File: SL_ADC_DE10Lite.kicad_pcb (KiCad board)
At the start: 4 copper layers, 25 parts, among them J1 DE10Lite header, J2 Conn_02x08_Odd_Even, J3 Digital ground header, J4 Analog header, J5 Power header

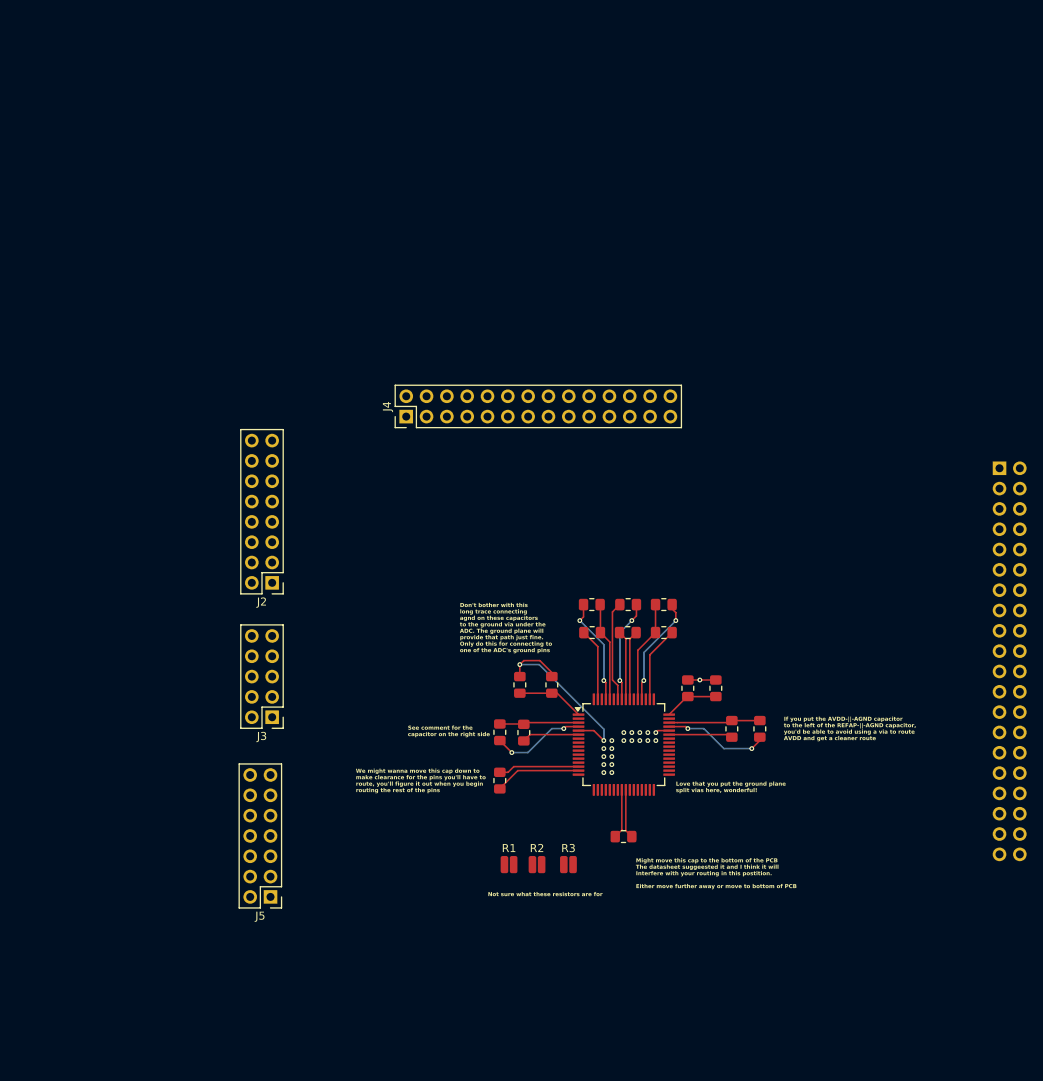
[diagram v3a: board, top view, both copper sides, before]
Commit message: Add De10lite dimensions and routes
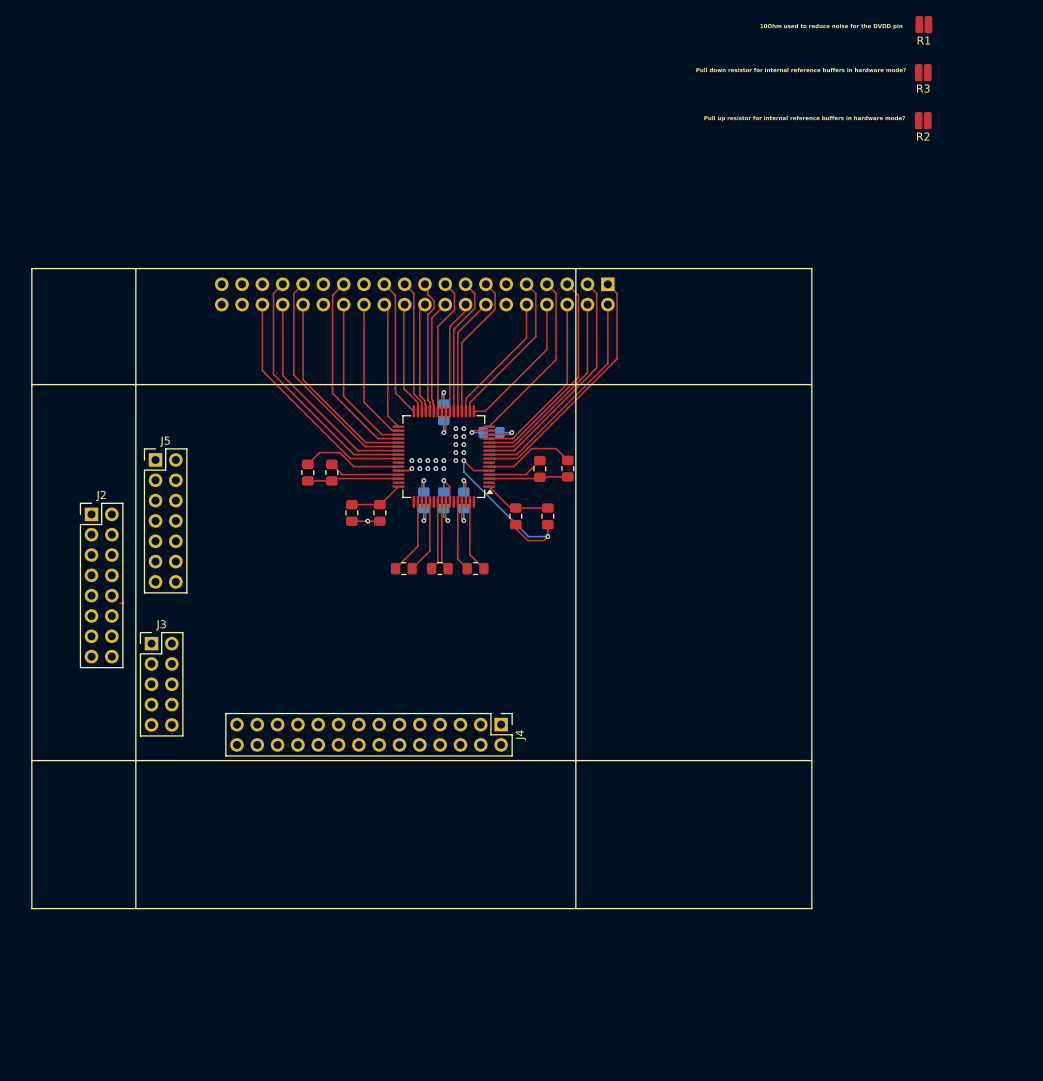
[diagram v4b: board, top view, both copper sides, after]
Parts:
- C10, C11, C2, C4, C5: moved to B.Cu
- J2: value Conn_02x08_Odd_Even -> Channel test headers
- moved R1 117.1 mm to (172.0, 20.0), turned to 180 degrees
- moved R3 108.5 mm to (171.9, 26.0), turned to 180 degrees
- moved R2 104.8 mm to (171.9, 32.0), turned to 180 degrees
- moved C3 62.4 mm to (98.0, 76.0), turned to -90 degrees
- moved C8 61.9 mm to (95.0, 76.0), turned to -90 degrees
- moved C5 57.6 mm to (112.0, 68.5), turned to -90 degrees
- moved J5 56.5 mm to (76.0, 74.4), turned to 0 degrees
- moved J1 54.1 mm to (132.5, 52.5), turned to 90 degrees
- moved C18 50.5 mm to (100.5, 81.0), turned to -90 degrees
- moved C20 44.3 mm to (104.0, 81.0), turned to -90 degrees
- moved C2 43.5 mm to (118.0, 71.0), turned to 180 degrees
- moved IC1 42.5 mm to (112.0, 74.0), turned to 180 degrees
- moved J4 40.3 mm to (119.2, 107.5), turned to -90 degrees
- moved C9 33.5 mm to (107.0, 88.0), turned to 0 degrees
- moved C24 33.5 mm to (127.5, 75.5), turned to -90 degrees
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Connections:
- IC1 pad 51: unconnected-(IC1-AGND-Pad51) -> /AGND
- J1 pad 1: /~{RD} -> /GPIO(19)-~{PAR}/SER
- J1 pad 10: /DB8 -> /DB12
- J1 pad 13: /DB7 -> /DB11
- J1 pad 14: /DB6 -> /DB10
- J1 pad 15: /DB5 -> /DB9
- J1 pad 16: /DB4 -> /DB8
- J1 pad 17: /DB3 -> /DB7
- J1 pad 18: /DB2 -> /DB6
- J1 pad 19: /DB1 -> /DB5
- J1 pad 2: /~{CS}/~{F5} -> /GPIO(24)-~{STBY}
- J1 pad 20: /DB0 -> /DB4
- J1 pad 21: /ASLEEP -> /DB3
- J1 pad 22: /GPIO(19)-~{PAR}/SER -> /DB2
- J1 pad 23: /GPIO(20)-BUSY/INT -> /DB1
- J1 pad 24: /GPIO(21)-RANGE/XCLK -> /DB0
- J1 pad 25: /GPIO(22)-~{HW}/SW -> unconnected-(J1-Pin_25-Pad25)
- J1 pad 26: /GPIO(23)-REFEN/~{WR} -> /GPIO(20)-BUSY/INT
- J1 pad 27: /GPIO(24)-~{STBY} -> /GPIO(21)-RANGE/XCLK
- J1 pad 28: /GPIO(25)-RESET -> /ASLEEP
- J1 pad 3: /DB15 -> /GPIO(25)-RESET
- J1 pad 35: unconnected-(J1-Pin_35-Pad35) -> /I2C5
- J1 pad 36: unconnected-(J1-Pin_36-Pad36) -> /GPIO(22)-~{HW}/SW
- J1 pad 37: unconnected-(J1-Pin_37-Pad37) -> /I2C3
- J1 pad 38: unconnected-(J1-Pin_38-Pad38) -> /I2C2
- J1 pad 39: unconnected-(J1-Pin_39-Pad39) -> /I2C1
- J1 pad 4: /DB14 -> /GPIO(23)-REFEN/~{WR}
- J1 pad 40: unconnected-(J1-Pin_40-Pad40) -> /I2C4
- J1 pad 5: /DB13 -> /~{RD}
- J1 pad 6: /DB12 -> /~{CS}/~{F5}
- J1 pad 7: /DB11 -> /DB15
- J1 pad 8: /DB10 -> /DB14
- J1 pad 9: /DB9 -> /DB13
- J4 pad 1: /AVDD -> /HVDD
- J4 pad 10: /HVDD -> unconnected-(J4-Pin_10-Pad10)
- J4 pad 11: /HVSS -> unconnected-(J4-Pin_11-Pad11)
- J4 pad 12: /HVSS -> unconnected-(J4-Pin_12-Pad12)
- J4 pad 13: /CH_D1 -> unconnected-(J4-Pin_13-Pad13)
- J4 pad 14: /CH_D1 -> unconnected-(J4-Pin_14-Pad14)
- J4 pad 15: /CH_D0 -> unconnected-(J4-Pin_15-Pad15)
- J4 pad 16: /CH_D0 -> /I2C5
- J4 pad 17: /CH_C1 -> /I2C4
- J4 pad 18: /CH_C1 -> /I2C3
- J4 pad 19: /CH_C0 -> /I2C2
- J4 pad 2: /AVDD -> /HVDD
- J4 pad 20: /CH_C0 -> /I2C1
- J4 pad 21: /CH_B1 -> /CH_D1
- J4 pad 22: /CH_B1 -> /CH_D0
- J4 pad 23: /CH_B0 -> /CH_C1
- J4 pad 24: /CH_B0 -> /CH_C0
- J4 pad 25: /CH_A1 -> /CH_B1
- J4 pad 26: /CH_A1 -> /CH_B0
- J4 pad 27: /CH_A0 -> /CH_A1
- J4 pad 3: /DVDD -> /HVSS
- J4 pad 4: /DVDD -> /HVSS
- J4 pad 7: /DGND -> unconnected-(J4-Pin_7-Pad7)
- J4 pad 8: /DGND -> unconnected-(J4-Pin_8-Pad8)
- J4 pad 9: /HVDD -> unconnected-(J4-Pin_9-Pad9)
- R3 pad 2: /AGND -> /DGND
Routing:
- net /AVDD: track 75.2 -> 32.4 mm, vias 10 -> 4
- net /GPIO(29)-CONVSTD: track 0.00 -> 31.5 mm
- net /GPIO(19)-~{PAR}/SER: track 0.00 -> 31.0 mm
- net /GPIO(22)-~{HW}/SW: track 0.00 -> 29.8 mm
- net /GPIO(25)-RESET: track 0.00 -> 28.7 mm
- net /GPIO(27)-CONVSTB: track 0.00 -> 28.6 mm
- net /GPIO(28)-CONVSTC: track 0.00 -> 27.2 mm
- net /GPIO(24)-~{STBY}: track 0.00 -> 26.9 mm
- net /~{RD}: track 0.00 -> 26.7 mm
- net /ASLEEP: track 0.00 -> 24.8 mm
- net /GPIO(23)-REFEN/~{WR}: track 0.00 -> 24.6 mm
- net /GPIO(26)-CONVSTA: track 0.00 -> 24.6 mm
- net /~{CS}/~{F5}: track 0.00 -> 22.5 mm
- net /DB15: track 0.00 -> 21.7 mm
- net /GPIO(20)-BUSY/INT: track 0.00 -> 20.3 mm
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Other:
- board text added: "10Ohm used to reduce noise for the DVDD pin"
- board text added: "Pull down resistor for internal reference buffers in hardware mode?"
- board text added: "Pull up resistor for internal reference buffers in hardware mode?"
- board text removed: "Don't bother with this long trace connecting agnd on these capacitors to the ground via under the ADC. The ground plane will provide that path just fine. Only do this for connecting to one of the ADC's ground pins"
- board text removed: "If you put the AVDD-||-AGND capacitor to the left of the REFAP-||-AGND capacitor, you'd be able to avoid using a via to route AVDD and get a cleaner route"
- board text removed: "Love that you put the ground plane split vias here, wonderful!"
- board text removed: "Might move this cap to the bottom of the PCB The datasheet suggeested it and I think it will Interfere with your routing in this postition. Either move further away or move to bottom of PCB"
- board text removed: "Not sure what these resistors are for"
- board text removed: "See comment for the capacitor on the right side"
- board text removed: "We might wanna move this cap down to make clearance for the pins you'll have to route, you'll figure it out when you begin routing the rest of the pins"

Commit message: Define separate AGND and DGND copper fill
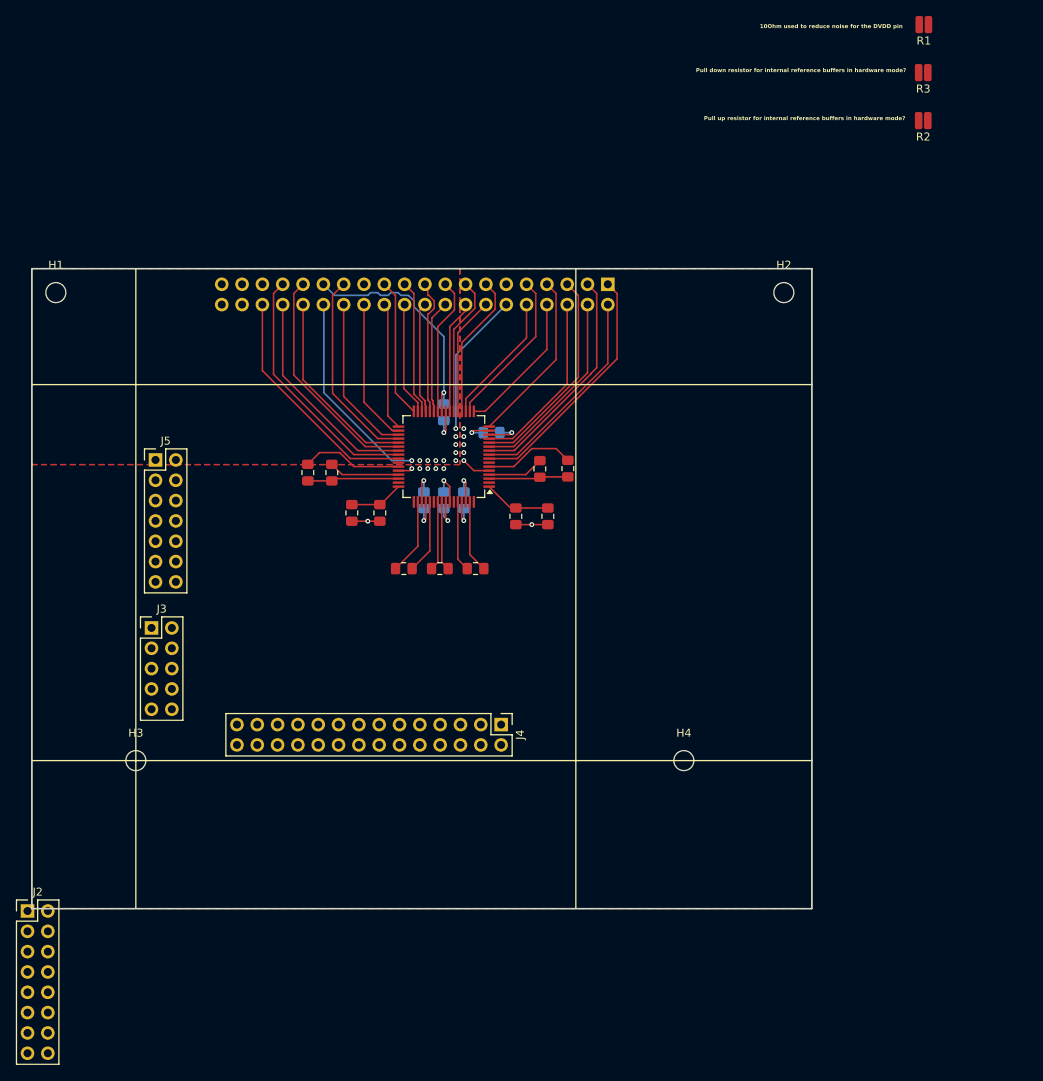
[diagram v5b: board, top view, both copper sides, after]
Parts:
- added H1: MountingHole, MountingHole:MountingHole_2.5mm, F.Cu at (63.5, 53.5)
- added H2: MountingHole, MountingHole:MountingHole_2.5mm, F.Cu at (154.5, 53.5)
- added H3: MountingHole, MountingHole:MountingHole_2.5mm, F.Cu at (73.5, 112.0)
- added H4: MountingHole, MountingHole:MountingHole_2.5mm, F.Cu at (142.0, 112.0)
- moved J2 50.2 mm to (60.0, 130.8)
- moved J3 1.96 mm to (75.5, 95.4)
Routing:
- net /DGND: track 4.27 -> 47.9 mm, vias 1 -> 3
- net /DVDD: track 3.87 -> 29.6 mm
- net /AGND: track 87.0 -> 68.9 mm
- net (no net): track 0.50 -> 0.00 mm, vias 18 -> 16
- added copper zone on F.Cu, net /AGND
- added copper zone on F.Cu, net /DGND
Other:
- board outline added: 97.5 x 80 mm

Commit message: Recent changes
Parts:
- removed J2: Channel test headers, Connector_PinHeader_2.54mm:PinHeader_2x08_P2.54mm_Vertical
- removed J3: Digital ground header, Connector_PinHeader_2.54mm:PinHeader_2x05_P2.54mm_Vertical
- removed J5: Power header, Connector_PinHeader_2.54mm:PinHeader_2x07_P2.54mm_Vertical
- added J6: Testing header, Connector_PinHeader_2.54mm:PinHeader_2x14_P2.54mm_Horizontal, F.Cu at (81.2, 101.5)
- moved R2 0.58 mm to (171.3, 32.0)
- moved R3 0.58 mm to (171.3, 26.0)
- moved R1 0.57 mm to (171.4, 20.0)
- moved J1 0.26 mm to (132.8, 52.5)
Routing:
- net /AGND: track 68.9 -> 80.1 mm, vias 8 -> 15
- net /DGND: vias 3 -> 11
- net (no net): vias 16 -> 0
- added copper zone on In2.Cu, net /AGND
- added copper zone on In1.Cu, net /DGND
- removed copper zone on F.Cu, net /AGND
- removed copper zone on F.Cu, net /DGND
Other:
- board size 97.5 x 80 mm -> 97.5 x 66.5 mm

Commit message: Updated version
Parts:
- removed J4: Analog header, Connector_PinHeader_2.54mm:PinHeader_2x14_P2.54mm_Vertical
- removed J6: Testing header, Connector_PinHeader_2.54mm:PinHeader_2x14_P2.54mm_Horizontal
- added J2: Conn_02x14_Odd_Even, Connector_PinHeader_2.54mm:PinHeader_2x14_P2.54mm_Vertical, F.Cu at (89.1, 110.0)
- added J3: Conn_02x04_Odd_Even, Connector_PinHeader_2.54mm:PinHeader_2x04_P2.54mm_Horizontal, F.Cu at (87.5, 103.1)

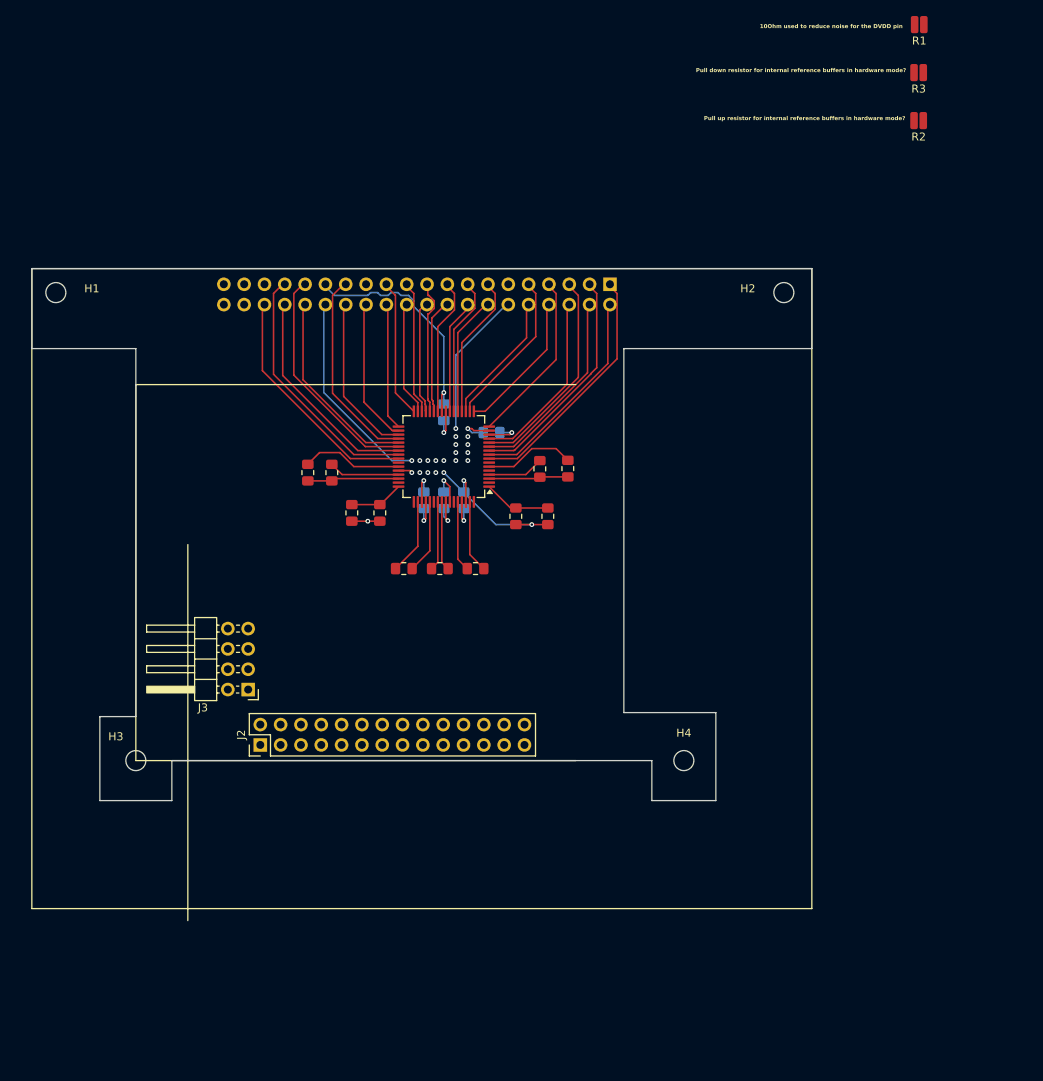
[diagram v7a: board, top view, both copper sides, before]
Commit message: Rounded corners!!!
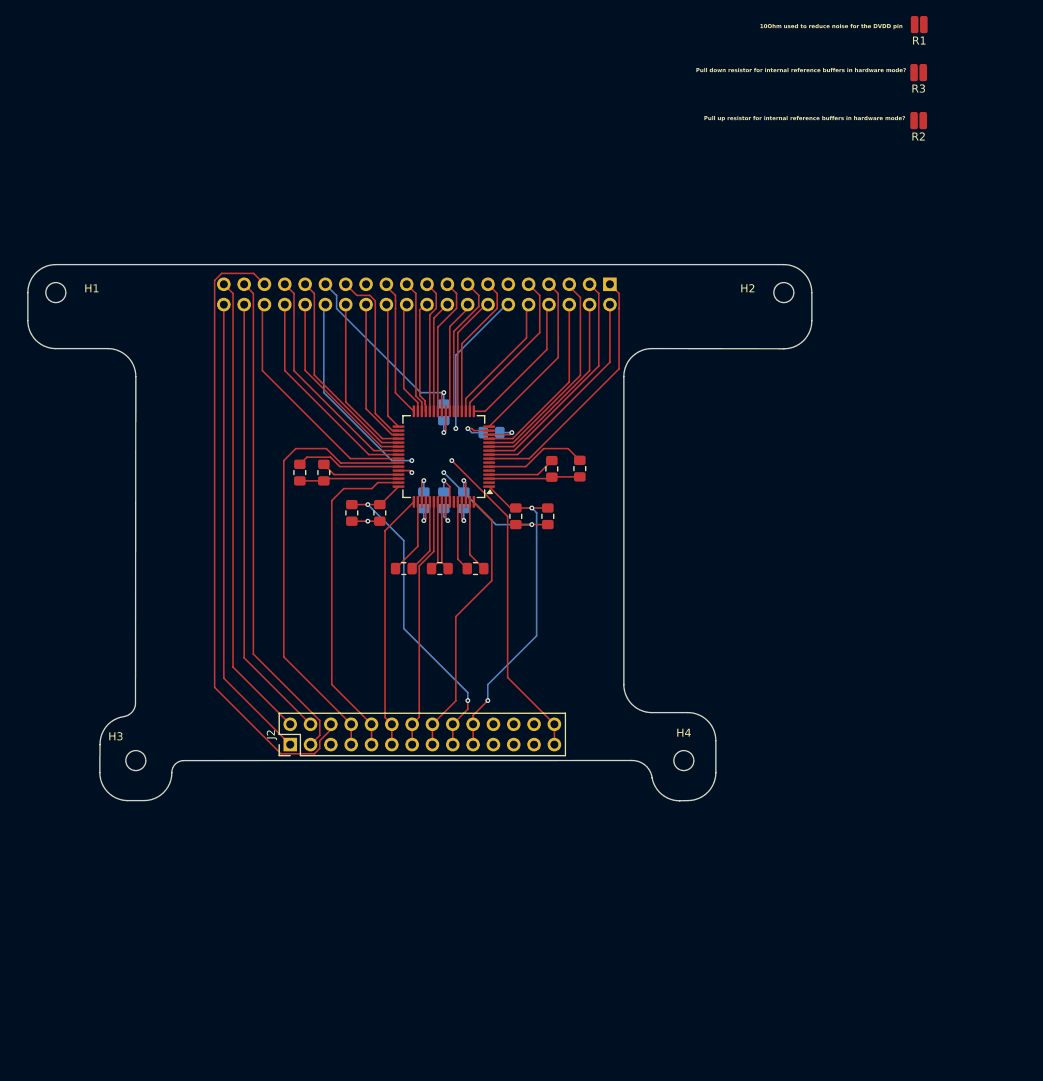
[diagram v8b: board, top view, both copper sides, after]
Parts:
- removed J3: Conn_02x04_Odd_Even, Connector_PinHeader_2.54mm:PinHeader_2x04_P2.54mm_Horizontal
- J2: value Conn_02x14_Odd_Even -> Analog header
- moved J2 3.74 mm to (92.8, 110.0)
- moved C1 1.50 mm to (125.5, 75.5)
- moved C24 1.50 mm to (129.0, 75.5)
- moved C3 1.00 mm to (97.0, 76.0)
- moved C8 1.00 mm to (94.0, 76.0)
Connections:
- J2 pad 1: /DVDD -> /I2C4
- J2 pad 10: /I2C5 -> /CH_A1
- J2 pad 11: /AGND -> /CH_B0
- J2 pad 12: unconnected-(J2-Pin_12-Pad12) -> /CH_B0
- J2 pad 13: /AGND -> /CH_B1
- J2 pad 14: /CH_A0 -> /CH_B1
- J2 pad 15: /AGND -> /CH_C0
- J2 pad 16: /CH_A1 -> /CH_C0
- J2 pad 17: /AGND -> /HVDD
- J2 pad 18: /CH_B0 -> /HVDD
- J2 pad 19: /AGND -> /HVSS
- J2 pad 20: /CH_B1 -> /HVSS
- J2 pad 21: /HVSS -> /AGND
- J2 pad 22: /CH_C0 -> /AGND
- J2 pad 23: /HVSS -> /AGND
- J2 pad 24: /CH_C1 -> /AGND
- J2 pad 25: /HVDD -> /AGND
- J2 pad 26: /CH_D0 -> /AGND
- J2 pad 27: /HVDD -> /DGND
- J2 pad 28: /CH_D1 -> /DGND
- J2 pad 3: /DVDD -> /I2C3
- J2 pad 5: /AGND -> unconnected-(J2-Pin_5-Pad5)
- J2 pad 6: /I2C3 -> /I2C5
- J2 pad 7: /AGND -> /CH_A0
- J2 pad 8: /I2C4 -> /CH_A0
- J2 pad 9: /AGND -> /CH_A1
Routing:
- net /I2C5: track 0.00 -> 78.5 mm
- net /I2C3: track 0.00 -> 61.9 mm
- net /I2C4: track 0.00 -> 58.4 mm
- net /I2C1: track 0.00 -> 58.4 mm
- net /I2C2: track 0.00 -> 55.9 mm
- net /CH_A0: track 0.00 -> 54.4 mm
- net /CH_A1: track 0.00 -> 41.8 mm
- net /DGND: track 47.9 -> 88.7 mm, vias 11 -> 4
- net /HVDD: track 6.77 -> 42.7 mm, vias 0 -> 2
- net /CH_C0: track 0.00 -> 34.3 mm
- net /HVSS: track 8.50 -> 41.6 mm, vias 0 -> 2
- net /CH_B0: track 0.00 -> 32.2 mm
- net /CH_B1: track 0.00 -> 31.5 mm
- net /GPIO(27)-CONVSTB: track 28.6 -> 23.8 mm
- net /GPIO(29)-CONVSTD: track 31.5 -> 26.8 mm
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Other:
- board size 97.5 x 66.5 mm -> 98 x 67 mm
